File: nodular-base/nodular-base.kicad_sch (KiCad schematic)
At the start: 18 parts, among them J11 Conn_01x08_Pin, SW1 SW_Push, SW2 SW_Push, SW3 SW_Push, U1 ESP32-S3-PICO-1-N8R2

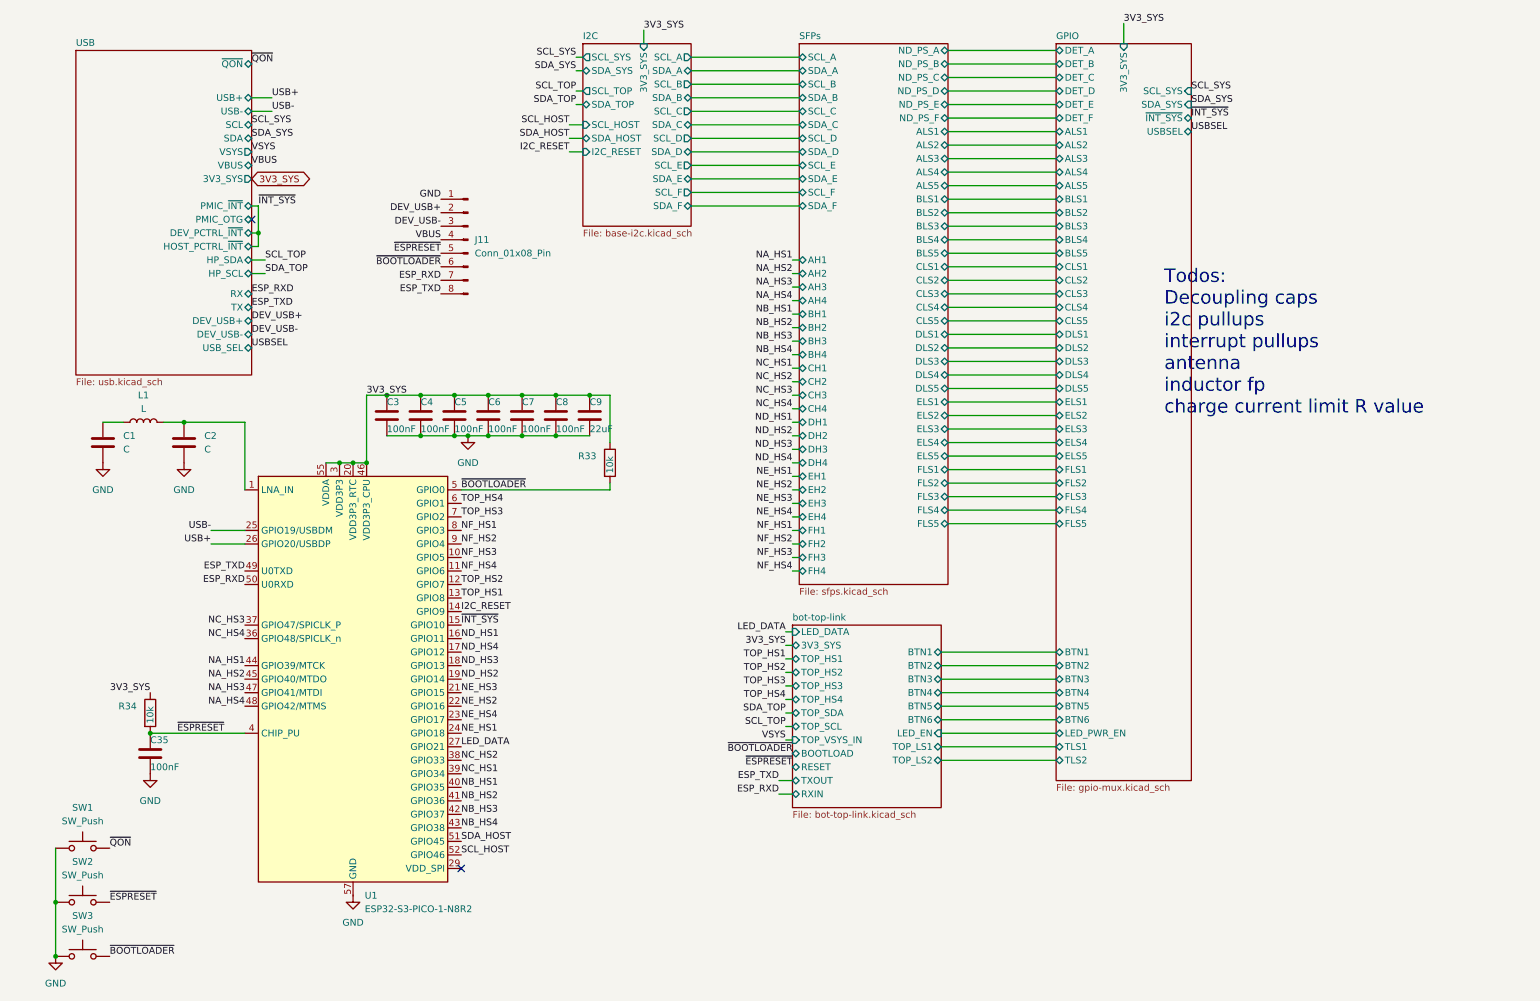
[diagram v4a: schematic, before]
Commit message: Add hole Add decoupling caps, pullups, and voltage dividers Set current limit on PMIC Determine battery attachment angle Update BOM and pinouts
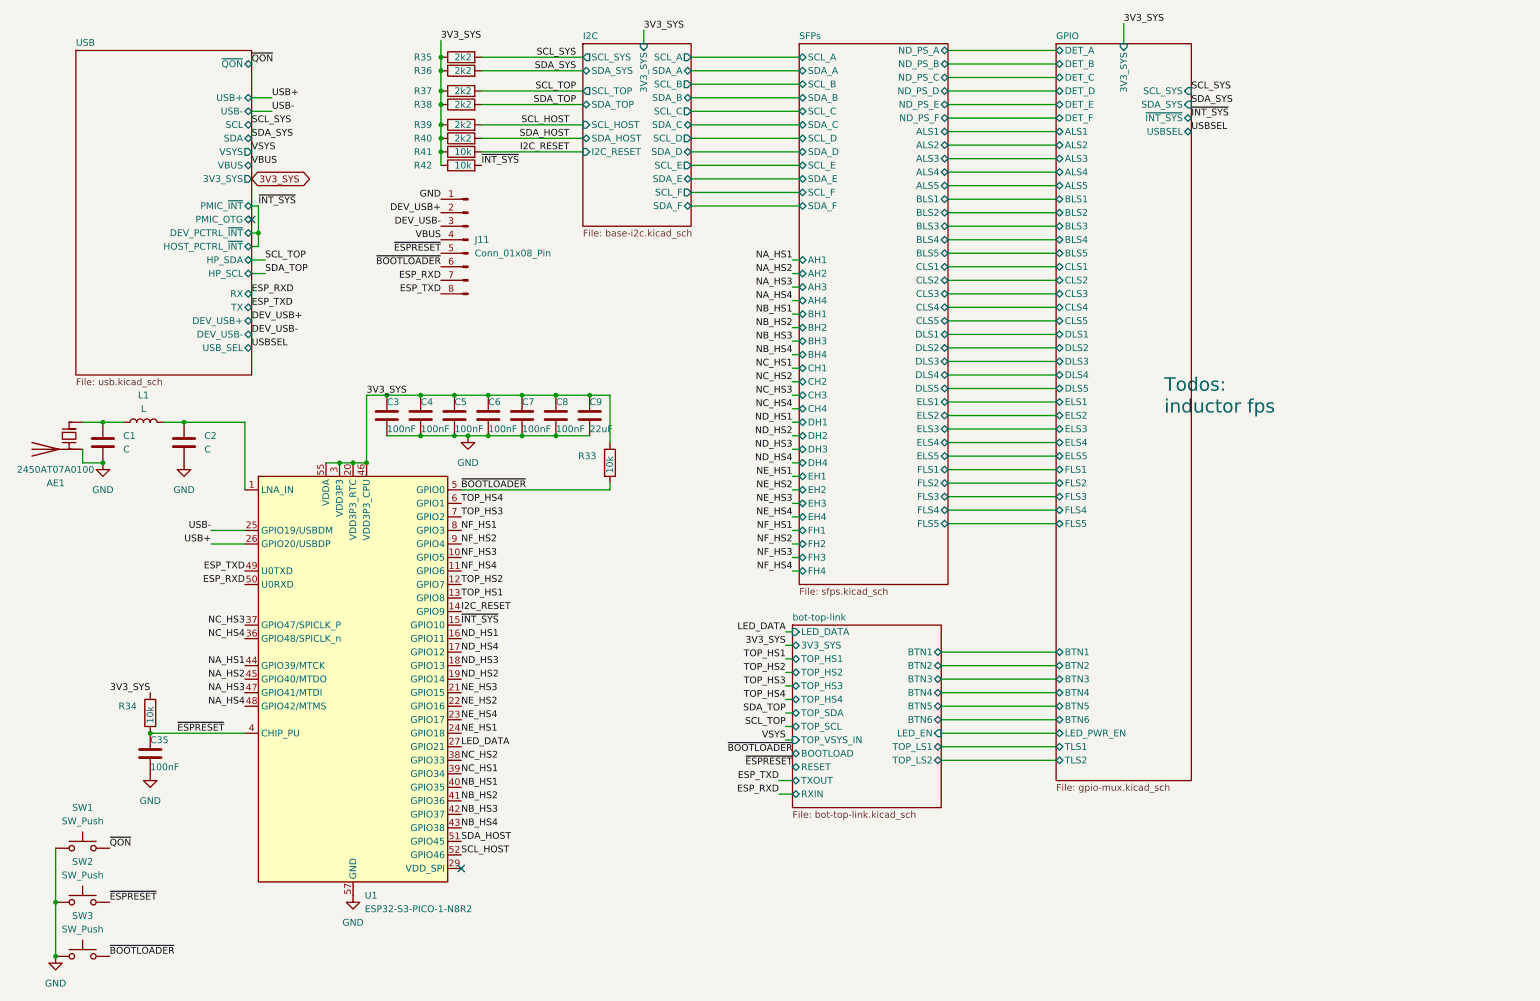
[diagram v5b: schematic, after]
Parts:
- added AE1: 2450AT07A0100, nodular:Johanson_2450AT07A0100_FLRight, symbol Device:Antenna_Chip
- added R35, R36, R37, R38, R39, R40: 2k2, Resistor_SMD:R_0402_1005Metric, symbol Device:R
- added R41, R42: 10k, Resistor_SMD:R_0402_1005Metric, symbol Device:R
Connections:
- net 3V3_SYS: now also R35.1, R36.1, R37.1, R38.1, R39.1, R40.1, R41.1, R42.1
- net GND: now also AE1.2 (PCB_Trace)
- net I2C_RESET: now also R41.2
- net SCL_HOST: now also R39.2
- net SCL_SYS: now also R35.2
- net SCL_TOP: now also R37.2
- net SDA_HOST: now also R40.2
- net SDA_SYS: now also R36.2
- net SDA_TOP: now also R38.2
- net ~{INT_SYS}: now also R42.2
- net at C1.1, L1.1: now also AE1.1 (FEED)
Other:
- note added: "Todos: inductor fps"
- note removed: "Todos: Decoupling caps i2c pullups interrupt pullups antenna inductor fp charge current limit R value"

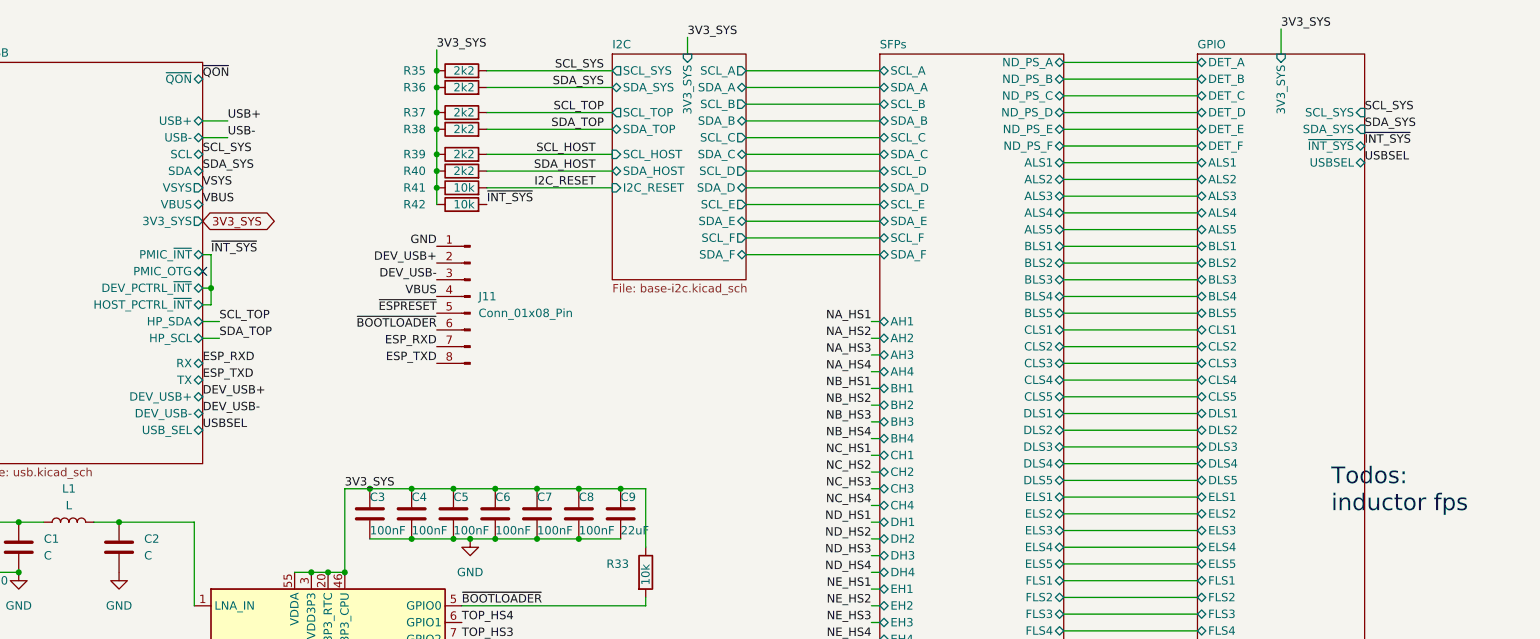
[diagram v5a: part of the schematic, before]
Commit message: Add VCONN support and load switch with 1.5A current limit on host port Add accelerometer interrupt connection Update BOM with important capacitor and inductor PNs and costings
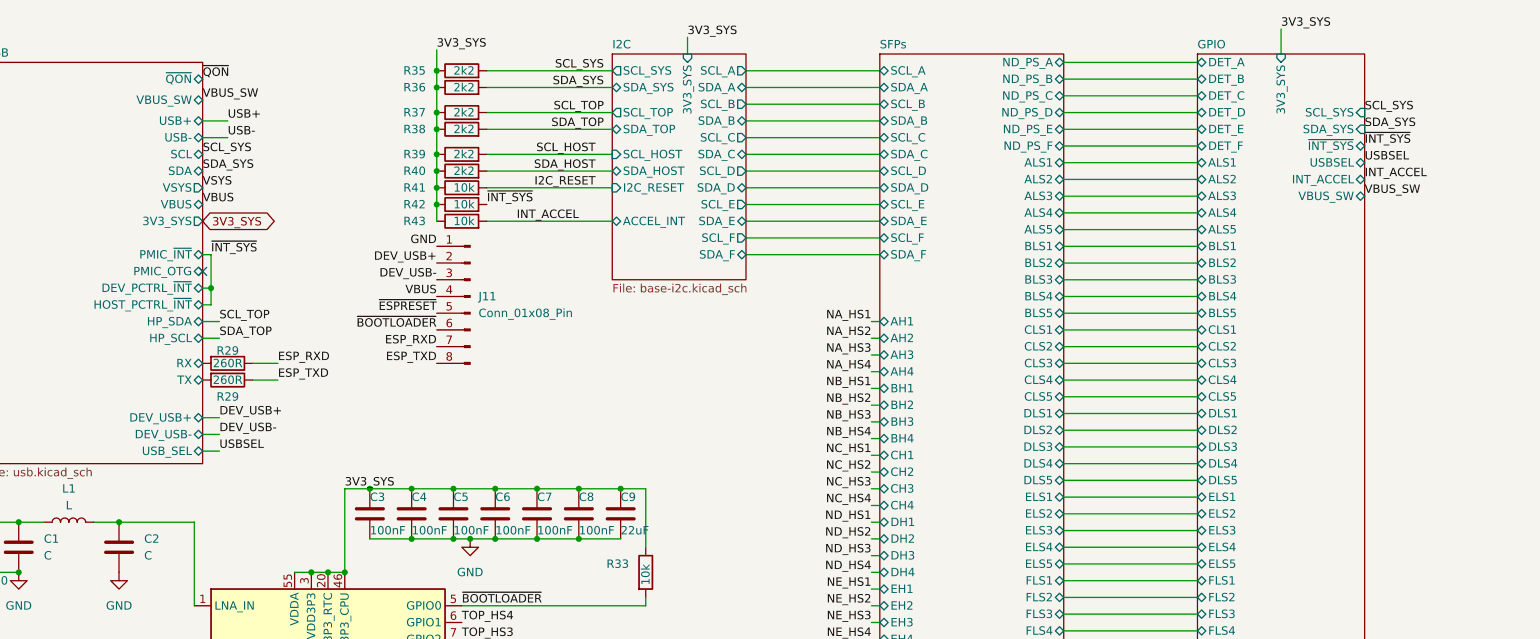
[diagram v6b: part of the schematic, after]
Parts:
- added R29 (x2): 260R, Resistor_SMD:R_0402_1005Metric, symbol Device:R
- added R43: 10k, Resistor_SMD:R_0402_1005Metric, symbol Device:R
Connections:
- net 3V3_SYS: now also R43.1
- net ESP_RXD: now also R29.1
- net ESP_TXD: now also R29.1
- new net INT_ACCEL: R43.2
- new net USB/RX: R29.2
- new net USB/TX: R29.2
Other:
- sheet GPIO ports: added INT_ACCEL, VBUS_SW; removed none
- sheet I2C ports: added ACCEL_INT; removed none
- sheet USB ports: added VBUS_SW; removed none
- note removed: "Todos: inductor fps"
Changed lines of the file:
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@@
   (junction (at 118.11 86.36) (diameter 0) (color 0 0 0 0)
+  )
+  (junction (at 90.17 43.18) (diameter 0) (color 0 0 0 0)
   )
   (junction (at 17.78 191.77) (diameter 0) (color 0 0 0 0)
@@
     (stroke (width 0) (type default))
   )
+  (wire (pts (xy 62.23 67.31) (xy 66.04 67.31))
+    (stroke (width 0) (type default))
+  )
   (wire (pts (xy 156.21 106.68) (xy 157.48 106.68))
     (stroke (width 0) (type default))
@@
     (stroke (width 0) (type default))
   )
+  (wire (pts (xy 54.61 80.645) (xy 57.15 80.645))
+    (stroke (width 0) (type default))
+  )
   (wire (pts (xy 54.61 33.02) (xy 58.42 33.02))
     (stroke (width 0) (type default))
@@
     (stroke (width 0) (type default))
   )
+  (wire (pts (xy 62.23 69.85) (xy 66.04 69.85))
+    (stroke (width 0) (type default))
+  )
   (wire (pts (xy 154.94 133.35) (xy 156.21 133.35))
     (stroke (width 0) (type default))
   )
+  (wire (pts (xy 54.61 75.565) (xy 57.15 75.565))
+    (stroke (width 0) (type default))
+  )
+  (wire (pts (xy 97.79 45.72) (xy 116.84 45.72))
+    (stroke (width 0) (type default))
+  )
   (wire (pts (xy 137.16 48.26) (xy 157.48 48.26))
     (stroke (width 0) (type default))
@@
     (stroke (width 0) (type default))
   )
+  (wire (pts (xy 90.17 43.18) (xy 90.17 45.72))
+    (stroke (width 0) (type default))
+  )
   (wire (pts (xy 71.12 99.06) (xy 73.66 99.06))
     (stroke (width 0) (type default))
@@
     (stroke (width 0) (type default))
   )
+  (wire (pts (xy 54.61 78.105) (xy 57.15 78.105))
+    (stroke (width 0) (type default))
+  )
   (wire (pts (xy 156.21 96.52) (xy 157.48 96.52))
     (stroke (width 0) (type default))
@@
     (stroke (width 0) (type default))
   )
-  (text "Todos:\ninductor fps\n" (at 226.06 90.17 0)
-    (effects (font (size 2.54 2.54)) (justify left bottom))
-  )
-  (label "DEV_USB+" (at 54.61 72.39 0) (fields_autoplaced)
+  (label "DEV_USB+" (at 57.15 75.565 0) (fields_autoplaced)
     (effects (font (size 1.27 1.27)) (justify left bottom))
   )
@@
     (effects (font (size 1.27 1.27)) (justify left bottom))
   )
-  (label "USBSEL" (at 54.61 77.47 0) (fields_autoplaced)
+  (label "USBSEL" (at 57.15 80.645 0) (fields_autoplaced)
     (effects (font (size 1.27 1.27)) (justify left bottom))
   )
@@
     (effects (font (size 1.27 1.27)) (justify right bottom))
   )
+  (label "VBUS_SW" (at 231.14 41.91 0) (fields_autoplaced)
+    (effects (font (size 1.27 1.27)) (justify left bottom))
+  )
   (label "NB_HS1" (at 93.98 160.02 0) (fields_autoplaced)
     (effects (font (size 1.27 1.27)) (justify left bottom))
@@
     (effects (font (size 1.27 1.27)) (justify left bottom))
   )
+  (label "INT_ACCEL" (at 231.14 39.37 0) (fields_autoplaced)
+    (effects (font (size 1.27 1.27)) (justify left bottom))
+  )
   (label "NA_HS4" (at 156.21 68.58 180) (fields_autoplaced)
     (effects (font (size 1.27 1.27)) (justify right bottom))
@@
     (effects (font (size 1.27 1.27)) (justify left bottom))
   )
+  (label "VBUS_SW" (at 54.61 27.305 0) (fields_autoplaced)
+    (effects (font (size 1.27 1.27)) (justify left bottom))
+  )
   (label "SDA_SYS" (at 54.61 38.1 0) (fields_autoplaced)
     (effects (font (size 1.27 1.27)) (justify left bottom))
@@
     (effects (font (size 1.27 1.27)) (justify right bottom))
   )
-  (label "ESP_RXD" (at 54.61 67.31 0) (fields_autoplaced)
+  (label "ESP_RXD" (at 66.04 67.31 0) (fields_autoplaced)
     (effects (font (size 1.27 1.27)) (justify left bottom))
   )
@@
     (effects (font (size 1.27 1.27)) (justify right bottom))
   )
+  (label "INT_ACCEL" (at 111.76 45.72 180) (fields_autoplaced)
+    (effects (font (size 1.27 1.27)) (justify right bottom))
+  )
   (label "NA_HS3" (at 53.34 142.24 180) (fields_autoplaced)
     (effects (font (size 1.27 1.27)) (justify right bottom))
@@
     (effects (font (size 1.27 1.27)) (justify right bottom))
   )
-  (label "ESP_TXD" (at 54.61 69.85 0) (fields_autoplaced)
+  (label "ESP_TXD" (at 66.04 69.85 0) (fields_autoplaced)
     (effects (font (size 1.27 1.27)) (justify left bottom))
   )
@@
     (effects (font (size 1.27 1.27)) (justify right bottom))
   )
-  (label "DEV_USB-" (at 54.61 74.93 0) (fields_autoplaced)
+  (label "DEV_USB-" (at 57.15 78.105 0) (fields_autoplaced)
     (effects (font (size 1.27 1.27)) (justify left bottom))
   )
@@
     )
   )
+  (symbol (lib_id "Device:R") (at 93.98 45.72 90) (unit 1)
+    (in_bom yes) (on_board yes) (dnp no)
+    (property "Reference" "R43" (at 85.09 45.72 90)
+      (effects (font (size 1.27 1.27)) (justify right))
+    )
+    (property "Value" "10k" (at 92.71 45.72 90)
+      (effects (font (size 1.27 1.27)) (justify right))
+    )
+    (property "Footprint" "Resistor_SMD:R_0402_1005Metric" (at 93.98 47.498 90)
+      (effects (font (size 1.27 1.27)) hide)
+    )
+    (property "Datasheet" "~" (at 93.98 45.72 0)
+      (effects (font (size 1.27 1.27)) hide)
+    )
+    (pin "1")
+    (pin "2")
+    (instances
+      (project "nodular-base"
+        (path "/6dcb0502-87e2-4c28-9ce8-81aab8925f06"
+          (reference "R43") (unit 1)
+        )
+      )
+    )
+  )
   (symbol (lib_id "Switch:SW_Push") (at 22.86 171.45 0) (unit 1)
     (in_bom yes) (on_board yes) (dnp no) (fields_autoplaced)
@@
         (path "/6dcb0502-87e2-4c28-9ce8-81aab8925f06"
           (reference "#PWR03") (unit 1)
+        )
+      )
+    )
+  )
+  (symbol (lib_id "Device:R") (at 58.42 67.31 270) (unit 1)
+    (in_bom yes) (on_board yes) (dnp no)
+    (property "Reference" "R29" (at 58.42 65.405 90)
+      (effects (font (size 1.27 1.27)))
+    )
+    (property "Value" "260R" (at 58.42 67.31 90)
+      (effects (font (size 1.27 1.27)))
+    )
+    (property "Footprint" "Resistor_SMD:R_0402_1005Metric" (at 58.42 65.532 90)
+      (effects (font (size 1.27 1.27)) hide)
+    )
+    (property "Datasheet" "~" (at 58.42 67.31 0)
+      (effects (font (size 1.27 1.27)) hide)
+    )
+    (pin "1")
+    (pin "2")
+    (instances
+      (project "nodular-base"
+        (path "/6dcb0502-87e2-4c28-9ce8-81aab8925f06/febeaf27-8aaa-445d-863a-3f8ee5c51d55"
+          (reference "R29") (unit 1)
+        )
+        (path "/6dcb0502-87e2-4c28-9ce8-81aab8925f06"
+          (reference "R44") (unit 1)
         )
       )
@@
     )
   )
+  (symbol (lib_id "Device:R") (at 58.42 69.85 270) (unit 1)
+    (in_bom yes) (on_board yes) (dnp no)
+    (property "Reference" "R29" (at 58.42 72.39 90)
+      (effects (font (size 1.27 1.27)))
+    )
+    (property "Value" "260R" (at 58.42 69.85 90)
+      (effects (font (size 1.27 1.27)))
+    )
+    (property "Footprint" "Resistor_SMD:R_0402_1005Metric" (at 58.42 68.072 90)
+      (effects (font (size 1.27 1.27)) hide)
+    )
+    (property "Datasheet" "~" (at 58.42 69.85 0)
+      (effects (font (size 1.27 1.27)) hide)
+    )
+    (pin "1")
+    (pin "2")
+    (instances
+      (project "nodular-base"
+        (path "/6dcb0502-87e2-4c28-9ce8-81aab8925f06/febeaf27-8aaa-445d-863a-3f8ee5c51d55"
+          (reference "R29") (unit 1)
+        )
+        (path "/6dcb0502-87e2-4c28-9ce8-81aab8925f06"
+          (reference "R45") (unit 1)
+        )
+      )
+    )
+  )
   (symbol (lib_id "Device:R") (at 35.56 146.05 0) (unit 1)
     (in_bom yes) (on_board yes) (dnp no)
@@
       (effects (font (size 1.27 1.27)) (justify right))
     )
+    (pin "INT_ACCEL" bidirectional (at 231.14 39.37 0)
+      (effects (font (size 1.27 1.27)) (justify right))
+    )
+    (pin "VBUS_SW" bidirectional (at 231.14 41.91 0)
+      (effects (font (size 1.27 1.27)) (justify right))
+    )
     (instances
       (project "nodular-base"
@@
       (effects (font (size 1.27 1.27)) (justify left))
     )
+    (pin "ACCEL_INT" bidirectional (at 116.84 45.72 180)
+      (effects (font (size 1.27 1.27)) (justify left))
+    )
     (instances
       (project "nodular-base"
@@
       (effects (font (size 1.27 1.27)) (justify right))
     )
-    (pin "DEV_USB+" bidirectional (at 54.61 72.39 0)
-      (effects (font (size 1.27 1.27)) (justify right))
-    )
-    (pin "DEV_USB-" bidirectional (at 54.61 74.93 0)
-      (effects (font (size 1.27 1.27)) (justify right))
-    )
-    (pin "USB_SEL" bidirectional (at 54.61 77.47 0)
-      (effects (font (size 1.27 1.27)) (justify right))
-    )
+    (pin "DEV_USB+" bidirectional (at 54.61 75.565 0)
+      (effects (font (size 1.27 1.27)) (justify right))
+    )
+    (pin "DEV_USB-" bidirectional (at 54.61 78.105 0)
+      (effects (font (size 1.27 1.27)) (justify right))
+    )
+    (pin "USB_SEL" bidirectional (at 54.61 80.645 0)
+      (effects (font (size 1.27 1.27)) (justify right))
+    )
+    (pin "VBUS_SW" bidirectional (at 54.61 27.305 0)
+      (effects (font (size 1.27 1.27)) (justify right))
+    )
